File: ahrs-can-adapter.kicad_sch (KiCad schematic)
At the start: 44 parts, among them J1 Flight Power, J2 Flight Telem, J3 CAN IN, J4 CAN OUT, SW1 Reset, U1 MPM3610-adafruit, U2 uA7805, U3 LTC2875-S8, U4 STM32F107R_B-C_Tx, U5 VCAN26A2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

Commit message: Fixed crystal circuit
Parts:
- U1: value MPM3610-adafruit -> MPM3610-adafruit 5V
- U2: value uA7805 -> UA78M33CDCYR
- U4: value STM32F107R_B-C_Tx -> STM32F107RCT6
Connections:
- net at C6.1: now also U4.5 (PD0), Y1.3; no longer Y1.2
- net at U4.6 (PD1), Y1.1: now also C5.1
- net at Y1.4: no longer C5.1
- no-connect marks 7 -> 9
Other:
- note removed: "UA78M33CDCYR"
- moved on the sheet: C6
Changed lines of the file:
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@@
 		)
 	)
-	(text "UA78M33CDCYR"
-		(exclude_from_sim no)
-		(at 90.297 26.416 0)
-		(effects
-			(font
-				(size 1.27 1.27)
-			)
-			(justify left bottom)
-		)
-	)
 	(text "CAN1\nConnected"
 		(exclude_from_sim no)
@@
 	)
 	(junction
+		(at 43.18 102.87)
+		(diameter 0)
+		(color 0 0 0 0)
+	)
+	(junction
 		(at 88.9 63.5)
 		(diameter 0)
@@
 	)
 	(junction
-		(at 45.72 113.03)
-		(diameter 0)
-		(color 0 0 0 0)
-	)
-	(junction
 		(at 182.88 111.76)
 		(diameter 0)
@@
 	)
 	(junction
+		(at 43.18 97.79)
+		(diameter 0)
+		(color 0 0 0 0)
+	)
+	(junction
+		(at 39.37 113.03)
+		(diameter 0)
+		(color 0 0 0 0)
+	)
+	(junction
 		(at 111.76 34.29)
 		(diameter 0)
@@
 	)
 	(no_connect
+		(at 45.72 100.33)
+	)
+	(no_connect
 		(at 157.48 109.22)
 	)
@@
 	)
 	(no_connect
+		(at 40.64 100.33)
+	)
+	(no_connect
 		(at 261.62 86.36)
 	)
@@
 	(wire
 		(pts
-			(xy 39.37 113.03) (xy 45.72 113.03)
-		)
-		(stroke
-			(width 0)
-			(type default)
-		)
-	)
-	(wire
-		(pts
 			(xy 91.44 63.5) (xy 93.98 63.5)
 		)
@@
 	(wire
 		(pts
-			(xy 39.37 105.41) (xy 39.37 100.33)
-		)
-		(stroke
-			(width 0)
-			(type default)
-		)
-	)
-	(wire
-		(pts
 			(xy 304.8 38.1) (xy 313.69 38.1)
 		)
@@
 	(wire
 		(pts
-			(xy 45.72 113.03) (xy 52.07 113.03)
-		)
-		(stroke
-			(width 0)
-			(type default)
-		)
-	)
-	(wire
-		(pts
 			(xy 175.26 152.4) (xy 190.5 152.4)
 		)
@@
 	(wire
 		(pts
-			(xy 45.72 114.3) (xy 45.72 113.03)
-		)
-		(stroke
-			(width 0)
-			(type default)
-		)
-	)
-	(wire
-		(pts
 			(xy 175.26 106.68) (xy 190.5 106.68)
 		)
@@
 	(wire
 		(pts
-			(xy 52.07 100.33) (xy 52.07 105.41)
+			(xy 259.08 140.97) (xy 259.08 134.62)
 		)
 		(stroke
@@
 	(wire
 		(pts
-			(xy 259.08 140.97) (xy 259.08 134.62)
+			(xy 27.94 97.79) (xy 43.18 97.79)
 		)
 		(stroke
@@
 	(wire
 		(pts
-			(xy 104.14 121.92) (xy 107.95 121.92)
+			(xy 27.94 113.03) (xy 39.37 113.03)
 		)
 		(stroke
@@
 	(wire
 		(pts
-			(xy 313.69 157.48) (xy 321.31 157.48)
+			(xy 104.14 121.92) (xy 107.95 121.92)
 		)
 		(stroke
@@
 	(wire
 		(pts
-			(xy 39.37 100.33) (xy 40.64 100.33)
+			(xy 313.69 157.48) (xy 321.31 157.48)
 		)
 		(stroke
@@
 	(wire
 		(pts
-			(xy 125.73 109.22) (xy 125.73 104.14)
+			(xy 39.37 102.87) (xy 43.18 102.87)
 		)
 		(stroke
@@
 	(wire
 		(pts
-			(xy 49.53 96.52) (xy 49.53 105.41)
+			(xy 125.73 109.22) (xy 125.73 104.14)
 		)
 		(stroke
@@
 	(wire
 		(pts
-			(xy 83.82 63.5) (xy 83.82 71.12)
+			(xy 49.53 96.52) (xy 49.53 105.41)
 		)
 		(stroke
@@
 	(wire
 		(pts
-			(xy 43.18 105.41) (xy 43.18 102.87)
+			(xy 83.82 63.5) (xy 83.82 71.12)
 		)
 		(stroke
@@
 	(wire
 		(pts
-			(xy 86.36 167.64) (xy 86.36 172.72)
+			(xy 43.18 105.41) (xy 43.18 102.87)
 		)
 		(stroke
@@
 	(wire
 		(pts
-			(xy 86.36 63.5) (xy 86.36 71.12)
+			(xy 86.36 167.64) (xy 86.36 172.72)
 		)
 		(stroke
@@
 	(wire
 		(pts
-			(xy 45.72 100.33) (xy 52.07 100.33)
+			(xy 86.36 63.5) (xy 86.36 71.12)
 		)
 		(stroke
@@
 	(wire
 		(pts
+			(xy 27.94 105.41) (xy 27.94 97.79)
+		)
+		(stroke
+			(width 0)
+			(type default)
+		)
+	)
+	(wire
+		(pts
 			(xy 43.18 93.98) (xy 43.18 97.79)
 		)
@@
 	(wire
 		(pts
+			(xy 39.37 102.87) (xy 39.37 105.41)
+		)
+		(stroke
+			(width 0)
+			(type default)
+		)
+	)
+	(wire
+		(pts
 			(xy 33.02 31.75) (xy 33.02 36.83)
 		)
@@
 	(wire
 		(pts
+			(xy 43.18 100.33) (xy 45.72 100.33)
+		)
+		(stroke
+			(width 0)
+			(type default)
+		)
+	)
+	(wire
+		(pts
 			(xy 175.26 106.68) (xy 175.26 116.84)
 		)
@@
 	(symbol
 		(lib_id "Device:C")
-		(at 52.07 109.22 0)
+		(at 27.94 109.22 0)
 		(unit 1)
 		(exclude_from_sim no)
@@
 		(fields_autoplaced yes)
 		(property "Reference" "C6"
-			(at 55.88 107.9499 0)
+			(at 31.75 107.9499 0)
 			(effects
 				(font
@@
 		)
 		(property "Value" "22pF"
-			(at 55.88 110.4899 0)
+			(at 31.75 110.4899 0)
 			(effects
 				(font
@@
 		)
 		(property "Footprint" "Capacitor_SMD:C_0603_1608Metric"
-			(at 53.0352 113.03 0)
+			(at 28.9052 113.03 0)
 			(effects
 				(font
@@
 		)
 		(property "Datasheet" "~"
-			(at 52.07 109.22 0)
+			(at 27.94 109.22 0)
 			(effects
 				(font
@@
 		)
 		(property "Description" "Unpolarized capacitor"
-			(at 52.07 109.22 0)
+			(at 27.94 109.22 0)
 			(effects
 				(font
@@
 			)
 		)
-		(property "Value" "uA7805"
+		(property "Value" "UA78M33CDCYR"
 			(at 99.06 30.48 0)
 			(effects
@@
 			)
 		)
-		(property "Value" "STM32F107R_B-C_Tx"
+		(property "Value" "STM32F107RCT6"
 			(at 91.0433 170.18 0)
 			(effects
@@
 			)
 		)
-		(property "Value" "MPM3610-adafruit"
+		(property "Value" "MPM3610-adafruit 5V"
 			(at 45.085 26.67 0)
 			(effects
@@
 		(lib_name "GND_6")
 		(lib_id "power:GND")
-		(at 45.72 114.3 0)
+		(at 39.37 113.03 0)
 		(unit 1)
 		(exclude_from_sim no)
@@
 		(fields_autoplaced yes)
 		(property "Reference" "#PWR019"
-			(at 45.72 120.65 0)
+			(at 39.37 119.38 0)
 			(effects
 				(font
@@
 		)
 		(property "Value" "GND"
-			(at 45.72 118.7434 0)
+			(at 39.37 117.4734 0)
 			(effects
 				(font
@@
 		)
 		(property "Footprint" ""
-			(at 45.72 114.3 0)
+			(at 39.37 113.03 0)
 			(effects
 				(font
@@
 		)
 		(property "Datasheet" ""
-			(at 45.72 114.3 0)
+			(at 39.37 113.03 0)
 			(effects
 				(font
@@
 		)
 		(property "Description" "Power symbol creates a global label with name \"GND\" , ground"
-			(at 45.72 114.3 0)
+			(at 39.37 113.03 0)
 			(effects
 				(font

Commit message: Changed flight board connectors
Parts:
- J1: footprint Connector_JST:JST_SH_BM06B-SRSS-TB_1x06-1MP_P1.00mm_Vertical -> Connector_JST:JST_GH_BM06B-GHS-TBT_1x06-1MP_P1.25mm_Vertical
- J2: footprint Connector_JST:JST_SH_BM04B-SRSS-TB_1x04-1MP_P1.00mm_Vertical -> Connector_JST:JST_GH_BM04B-GHS-TBT_1x04-1MP_P1.25mm_Vertical
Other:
- note added: "JST GH BM04B-GHS-TBT"
- note added: "JST GH BM06B-GHS-TBT"
- note removed: "JST SH"
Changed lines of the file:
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@@
 		)
 	)
-	(text "JST SH"
+	(text "JST GH BM04B-GHS-TBT"
 		(exclude_from_sim no)
-		(at 258.826 45.72 0)
+		(at 267.208 45.72 0)
 		(effects
 			(font
@@
 		)
 	)
-	(text "JST SH"
+	(text "JST GH BM06B-GHS-TBT"
 		(exclude_from_sim no)
-		(at 195.072 49.784 0)
+		(at 203.962 49.784 0)
 		(effects
 			(font
@@
 		)
 		(instances
-			(project ""
+			(project "ahrs-can-adapter"
 				(path "/d4189e78-aea6-4ab0-ae87-a95ad317149e"
 					(reference "J3")
@@
 		)
 		(instances
-			(project ""
+			(project "ahrs-can-adapter"
 				(path "/d4189e78-aea6-4ab0-ae87-a95ad317149e"
 					(reference "#PWR02")
@@
 		)
 		(instances
-			(project ""
+			(project "ahrs-can-adapter"
 				(path "/d4189e78-aea6-4ab0-ae87-a95ad317149e"
 					(reference "U4")
@@
 		)
 		(instances
-			(project ""
+			(project "ahrs-can-adapter"
 				(path "/d4189e78-aea6-4ab0-ae87-a95ad317149e"
 					(reference "J4")
@@
 		)
 		(instances
-			(project ""
+			(project "ahrs-can-adapter"
 				(path "/d4189e78-aea6-4ab0-ae87-a95ad317149e"
 					(reference "U1")
@@
 			)
 		)
-		(property "Footprint" "Connector_JST:JST_SH_BM06B-SRSS-TB_1x06-1MP_P1.00mm_Vertical"
+		(property "Footprint" "Connector_JST:JST_GH_BM06B-GHS-TBT_1x06-1MP_P1.25mm_Vertical"
 			(at 189.23 44.45 0)
 			(effects
@@
 		)
 		(instances
-			(project ""
+			(project "ahrs-can-adapter"
 				(path "/d4189e78-aea6-4ab0-ae87-a95ad317149e"
 					(reference "#PWR01")
@@
 		)
 		(instances
-			(project ""
+			(project "ahrs-can-adapter"
 				(path "/d4189e78-aea6-4ab0-ae87-a95ad317149e"
 					(reference "D2")
@@
 		)
 		(instances
-			(project ""
+			(project "ahrs-can-adapter"
 				(path "/d4189e78-aea6-4ab0-ae87-a95ad317149e"
 					(reference "D1")
@@
 		)
 		(instances
-			(project ""
+			(project "ahrs-can-adapter"
 				(path "/d4189e78-aea6-4ab0-ae87-a95ad317149e"
 					(reference "#PWR06")
@@
 			)
 		)
-		(property "Footprint" "Connector_JST:JST_SH_BM04B-SRSS-TB_1x04-1MP_P1.00mm_Vertical"
+		(property "Footprint" "Connector_JST:JST_GH_BM04B-GHS-TBT_1x04-1MP_P1.25mm_Vertical"
 			(at 252.73 40.64 0)
 			(effects
@@
 		)
 		(instances
-			(project ""
+			(project "ahrs-can-adapter"
 				(path "/d4189e78-aea6-4ab0-ae87-a95ad317149e"
 					(reference "J2")
@@
 		)
 		(instances
-			(project ""
+			(project "ahrs-can-adapter"
 				(path "/d4189e78-aea6-4ab0-ae87-a95ad317149e"
 					(reference "U3")

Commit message: Changed MCU to stm32g474ret6
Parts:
- removed U4: STM32F107RCT6, Package_QFP:LQFP-64_10x10mm_P0.5mm, symbol MCU_ST_STM32F1:STM32F107R_B-C_Tx
- added U4: STM32G474RETx, Package_QFP:LQFP-64_10x10mm_P0.5mm, symbol MCU_ST_STM32G4:STM32G474RETx
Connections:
- net +3.3V: now also U4.1 (VBAT), U4.16 (VDD), U4.28 (VREF+), U4.29 (VDDA), U4.32 (VDD), U4.48 (VDD), U4.64 (VDD)
- net Current: now also U4.20 (PA6)
- net GND: now also U4.15 (VSS), U4.27 (VSSA), U4.31 (VSS), U4.47 (VSS), U4.63 (VSS)
- net LED1: now also U4.24 (PB0)
- net LED2: now also U4.25 (PB1)
- net LED3: now also U4.26 (PB2)
- net NRST: now also U4.7 (PG10)
- net RX: now also U4.17 (PA3)
- net SWCLK: now also U4.50 (PA14)
- net SWDIO: now also U4.49 (PA13)
- net TX: now also U4.14 (PA2)
- net Voltage: now also U4.21 (PA7)
- net at C6.1, Y1.3: now also U4.5 (PF0)
- net at U6.1 (TXD): now also U4.35 (PB13)
- net at U6.4 (RXD): now also U4.34 (PB12)
- net at U3.4 (RXD): now also U4.45 (PA11)
- net at U3.1 (TXD): now also U4.46 (PA12)
- net at C5.1, Y1.1: now also U4.6 (PF1)

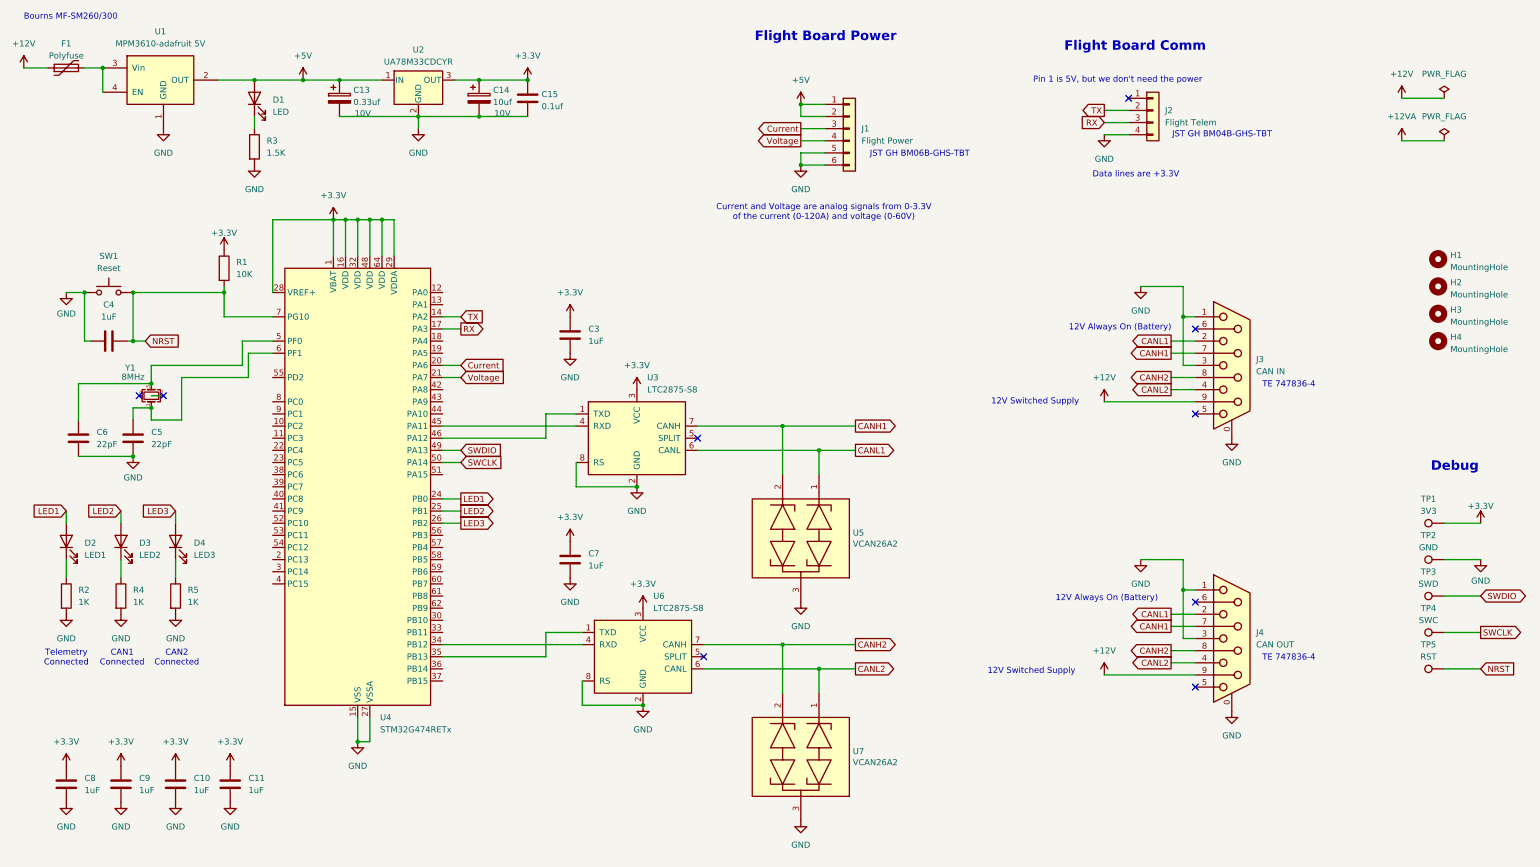
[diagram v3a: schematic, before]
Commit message: updated crystal circuit
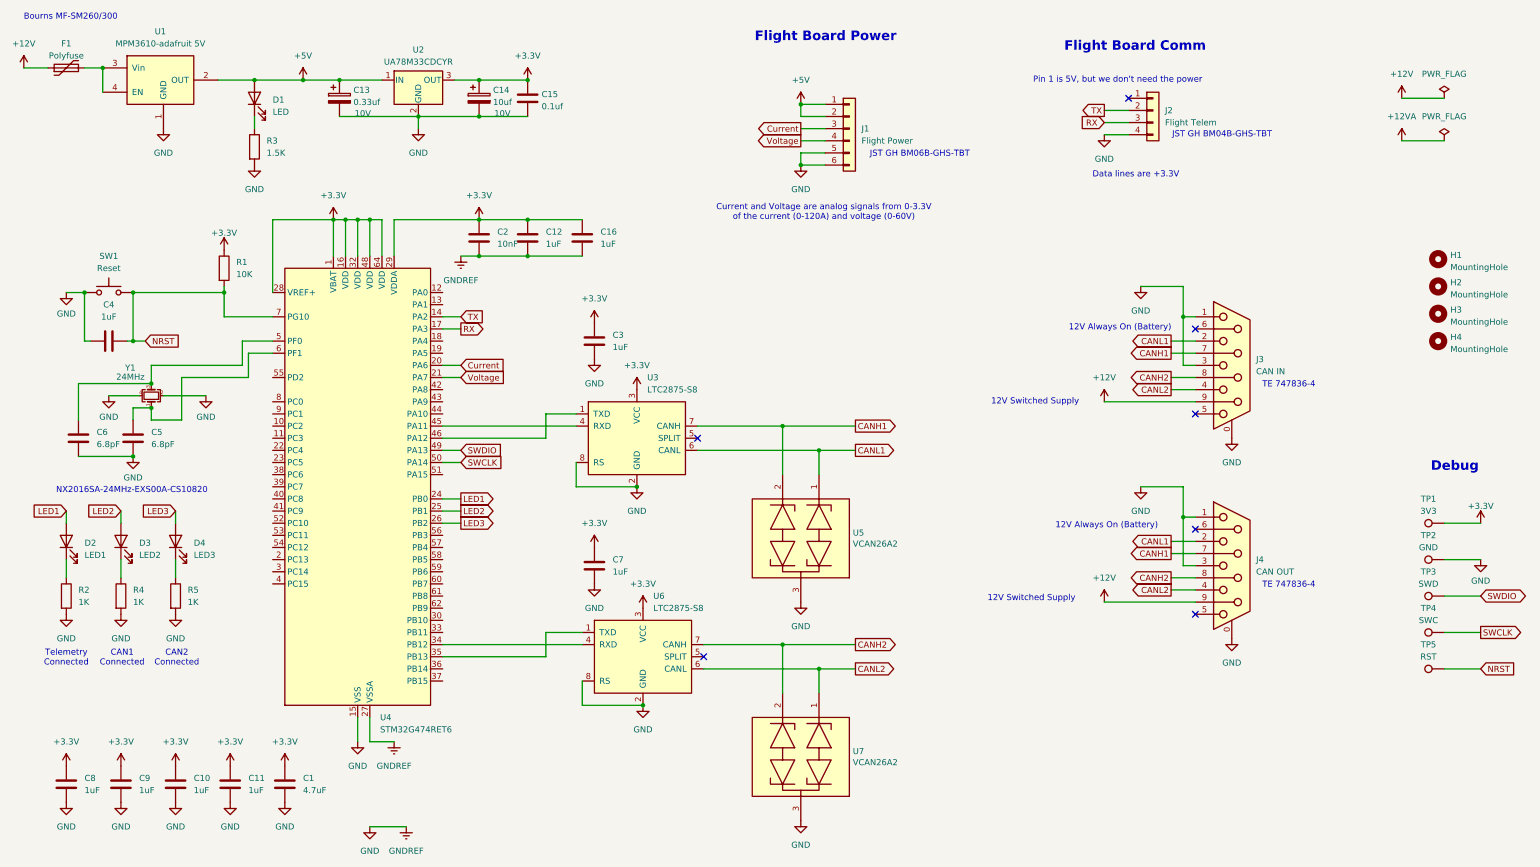
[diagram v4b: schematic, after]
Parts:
- added C1: 4.7uF, Capacitor_SMD:C_0603_1608Metric, symbol Device:C
- added C12, C16: 1uF, Capacitor_SMD:C_0603_1608Metric, symbol Device:C
- added C2: 10nF, Capacitor_SMD:C_0603_1608Metric, symbol Device:C
- C5, C6: value 22pF -> 6.8pF
- U4: value STM32G474RETx -> STM32G474RET6
- Y1: value 8MHz -> 24MHz; footprint Crystal:Crystal_SMD_TXC_7M-4Pin_3.2x2.5mm -> Crystal:Crystal_SMD_2016-4Pin_2.0x1.6mm
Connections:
- net +3.3V: now also C1.1, C12.1, C16.1, C2.1
- net GND: now also Y1.2, Y1.4, C1.2, C12.2, C16.2, C2.2
- no-connect marks 9 -> 7
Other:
- note added: "NX2016SA-24MHz-EXS00A-CS10820"
- moved on the sheet: C3, C7, J4

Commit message: Changed telemetry uart pins
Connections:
- net RX: now also U4.53 (PC11); no longer U4.17 (PA3)
- net TX: now also U4.52 (PC10); no longer U4.14 (PA2)
